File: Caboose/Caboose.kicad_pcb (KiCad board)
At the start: 2 copper layers, 47.5 x 21.5 mm, 0 parts

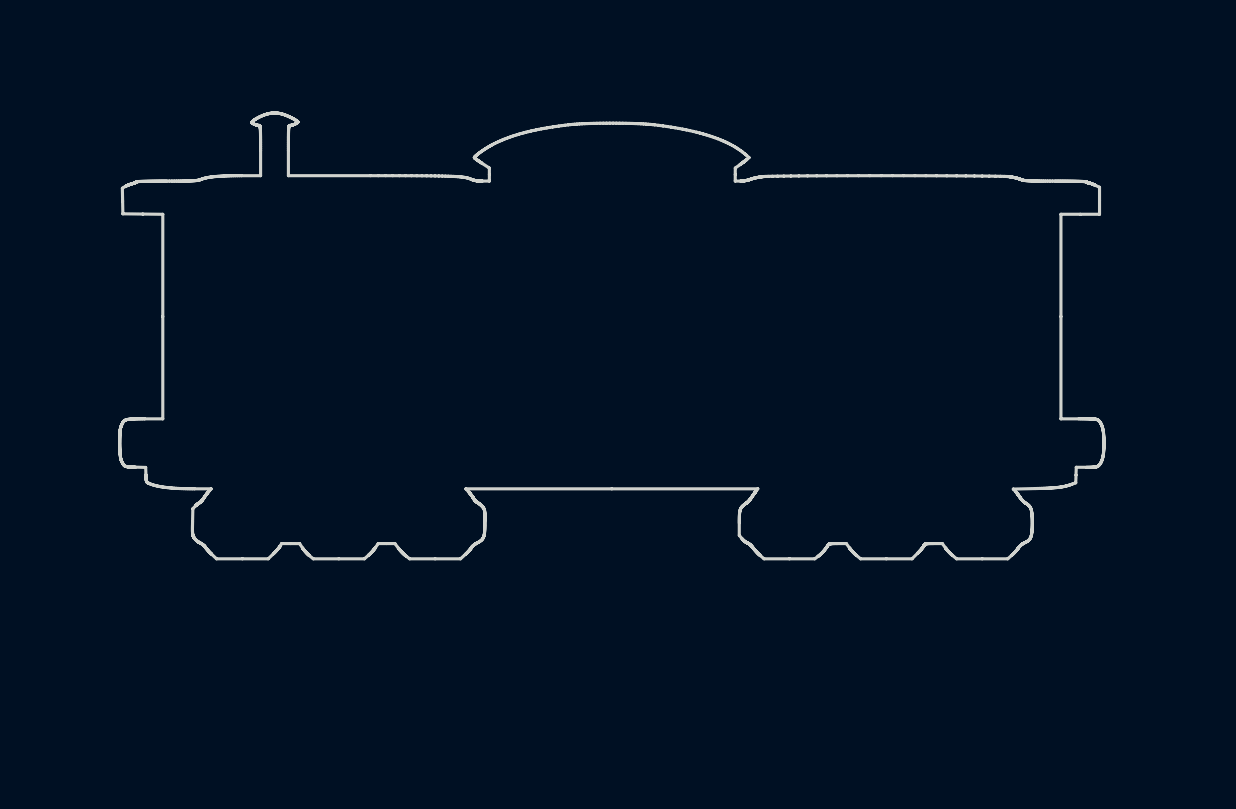
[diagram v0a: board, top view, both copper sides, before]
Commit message: Add & Align Pins
Add pins to all trains and set proper locations
Move RGB LEDs and resistors
Connect RGB LEDs to resistors and speaker to Arduino
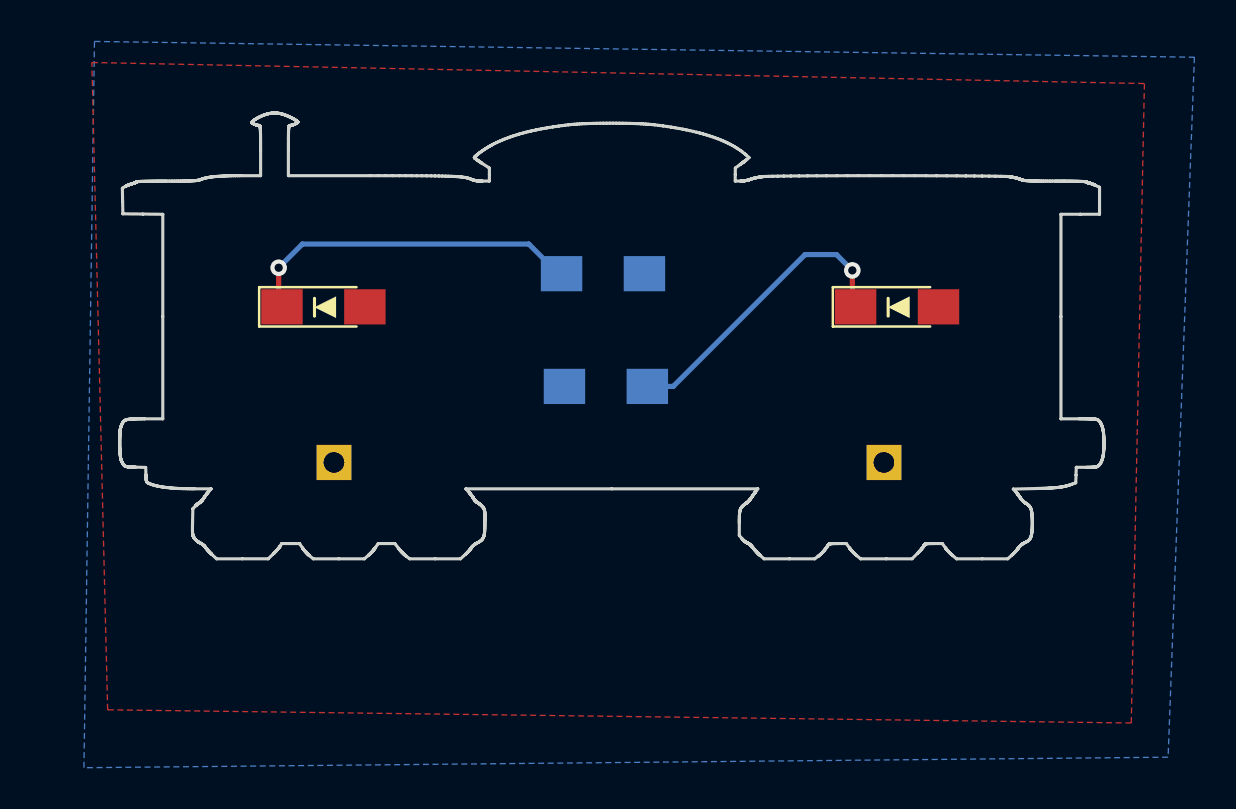
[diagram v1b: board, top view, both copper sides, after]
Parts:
- added D1: LED, LEDs:LED_1206_HandSoldering, F.Cu at (9.91, 80.5)
- added D2: LED, LEDs:LED_1206_HandSoldering, F.Cu at (37.6, 80.5)
- added MK1: VCC, Pin_Headers:Pin_Header_Angled_1x01_Pitch2.54mm, B.Cu at (10.4, 88.0)
- added MK2: GND, Pin_Headers:Pin_Header_Angled_1x01_Pitch2.54mm, B.Cu at (37.0, 88.0)
- added R1: R, Resistors_SMD:R_1206_HandSoldering, B.Cu at (23.4, 78.9)
- added R2: R, Resistors_SMD:R_1206_HandSoldering, B.Cu at (23.5, 84.3)
- added REF**: LED_1206, Markings:LED_1206, F.Cu at (37.6, 80.5)
- added REF**: LED_1206, Markings:LED_1206, F.Cu at (9.91, 80.5)
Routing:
- net Net-(D1-Pad1): track 0.00 -> 16.7 mm, vias 0 -> 1
- net Net-(D2-Pad1): track 0.00 -> 14.7 mm, vias 0 -> 1
- added copper zone on B.Cu, net /GND
- added copper zone on F.Cu, net /VCC

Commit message: Change Schematic For RGB LEDs
Add transistors to control 3 RGB LEDs
Add Silkscreen detail to caboose
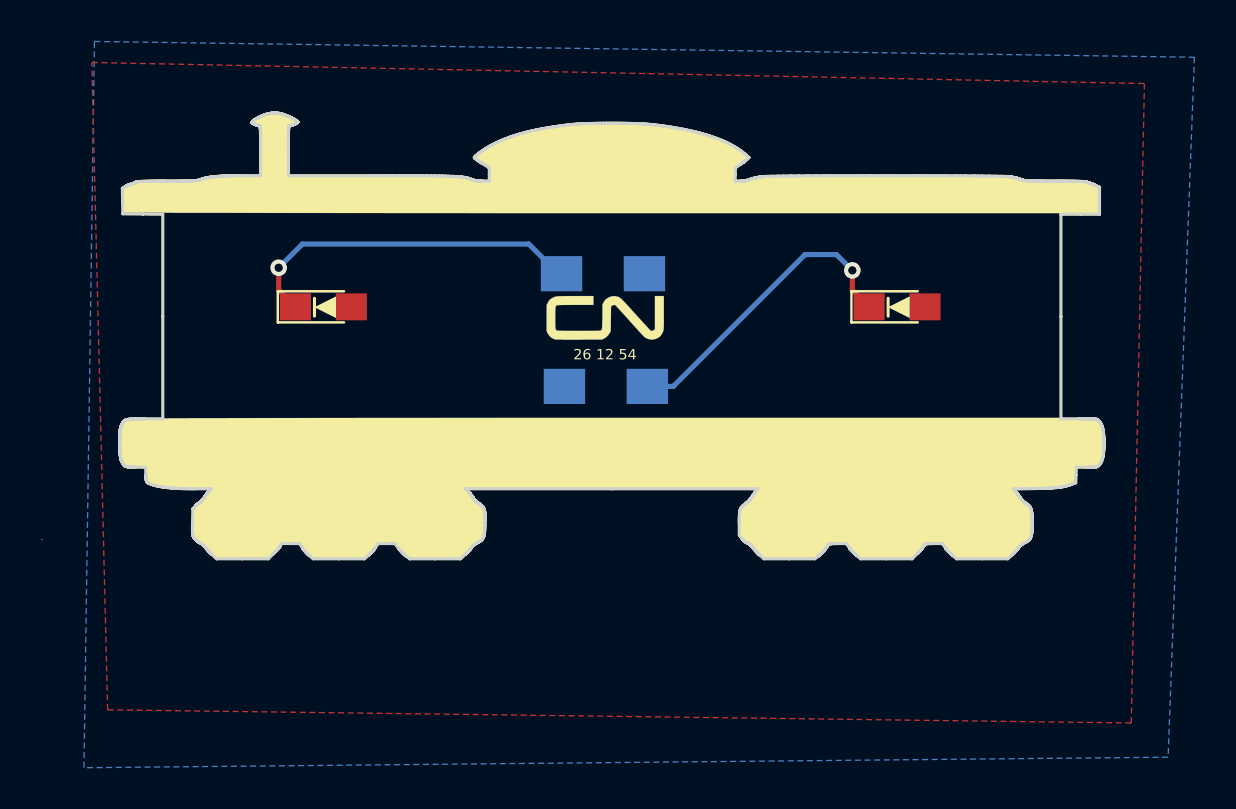
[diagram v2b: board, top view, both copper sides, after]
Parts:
- added G***: LOGO, silkscreen:CN-Small, F.Cu at (23.5, 81.0)
- added G***: LOGO, silkscreen:caboose, F.Cu at (24.1, 80.1)
- D1, D2: footprint LEDs:LED_1206_HandSoldering -> LEDs:LED_0805_HandSoldering
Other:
- board text added: "26 12 54"

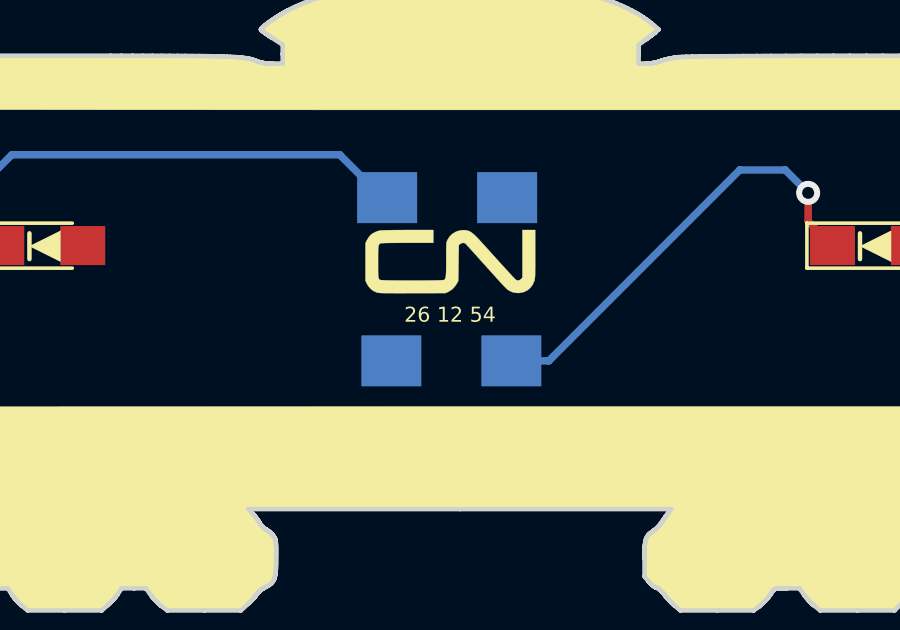
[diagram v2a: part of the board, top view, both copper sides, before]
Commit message: Finalize Tracks
Finish tracks for 3 RGB LEDs
Move date to locomotive, remove from caboose
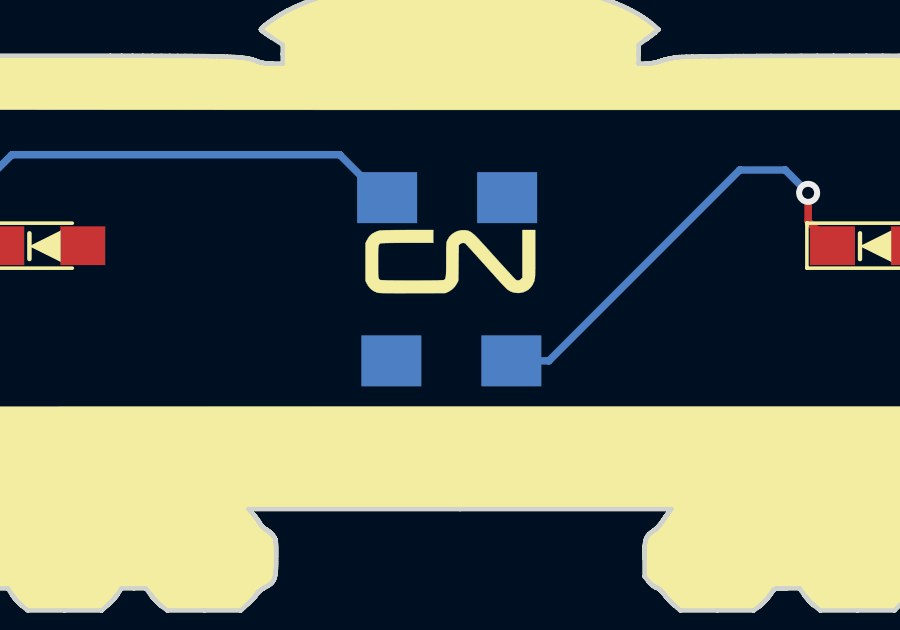
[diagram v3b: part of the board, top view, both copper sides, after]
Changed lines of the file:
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@@
-(kicad_pcb (version 20171130) (host pcbnew 5.0.0-rc2-dev-unknown-f73b9a5~65~ubuntu16.04.1)
+(kicad_pcb (version 20171130) (host pcbnew 5.0.0-rc2-dev-unknown-904eb82~65~ubuntu16.04.1)
   (general
     (thickness 1.6)
@@
     )
   )
-  (gr_text "26 12 54" (at 23.495 82.804) (layer F.SilkS)
+  (gr_text "26 12 54" (at 23.495 82.804) (layer F.Fab)
     (effects (font (size 0.5 0.5) (thickness 0.125)))
   )

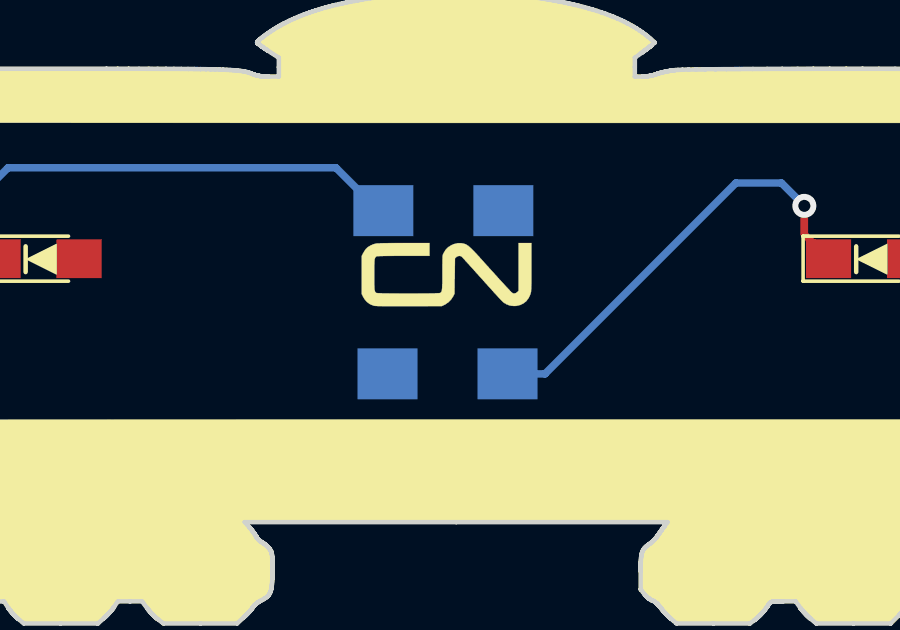
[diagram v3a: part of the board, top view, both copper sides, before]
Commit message: Update Text
Change dates on trains
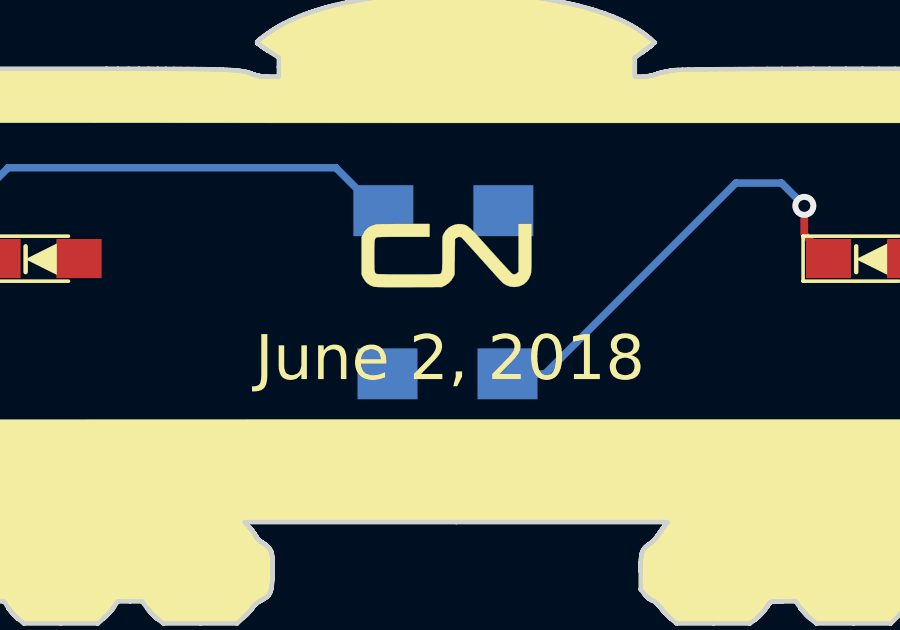
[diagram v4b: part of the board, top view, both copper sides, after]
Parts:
- moved G*** 0.63 mm to (23.5, 80.4)
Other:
- board text added: "155Ω"
- board text added: "June 2, 2018"
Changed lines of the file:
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@@
-(kicad_pcb (version 20171130) (host pcbnew 5.0.0-rc2-dev-unknown-904eb82~65~ubuntu16.04.1)
+(kicad_pcb (version 20171130) (host pcbnew 5.0.2-bee76a0~70~ubuntu18.04.1)
   (general
     (thickness 1.6)
-    (drawings 2411)
+    (drawings 2414)
     (tracks 14)
     (zones 0)
@@
     (pad_drill 0.762)
     (pad_to_mask_clearance 0.2)
+    (solder_mask_min_width 0.25)
     (aux_axis_origin 0 0)
     (visible_elements FFFFFF7F)
     (pcbplotparams
-      (layerselection 0x010fc_ffffffff)
-      (usegerberextensions false)
+      (layerselection 0x010f0_ffffffff)
+      (usegerberextensions true)
       (usegerberattributes false)
       (usegerberadvancedattributes false)
@@
       (hpglpennumber 1)
       (hpglpenspeed 20)
-      (hpglpendiameter 15)
+      (hpglpendiameter 15.000000)
       (psnegative false)
       (psa4output false)
@@
       (outputformat 1)
       (mirror false)
-      (drillshape 1)
+      (drillshape 0)
       (scaleselection 1)
-      (outputdirectory ""))
+      (outputdirectory "GERBER/"))
   )
   (net 0 "")
@@
   )
   (module silkscreen:CN-Small (layer F.Cu)
-    (at 23.495 81.026)
+    (at 23.495 80.391)
     (fp_text reference G*** (at 0 0) (layer F.SilkS) hide
       (effects (font (size 1.524 1.524) (thickness 0.3)))
@@
     )
   )
+  (gr_text "June 2, 2018" (at 23.622 83.82) (layer F.SilkS)
+    (effects (font (size 1.5 1.5) (thickness 0.3)))
+  )
+  (gr_text 155Ω (at 23.495 82.296) (layer B.SilkS)
+    (effects (font (size 1 1) (thickness 0.25)) (justify mirror))
+  )
+  (gr_text 155Ω (at 23.495 76.835) (layer B.SilkS)
+    (effects (font (size 1 1) (thickness 0.25)) (justify mirror))
+  )
   (gr_text "26 12 54" (at 23.495 82.804) (layer F.Fab)
